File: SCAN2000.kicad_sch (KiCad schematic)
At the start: 15 parts, among them J1 Conn_02x16_Row_Letter_First

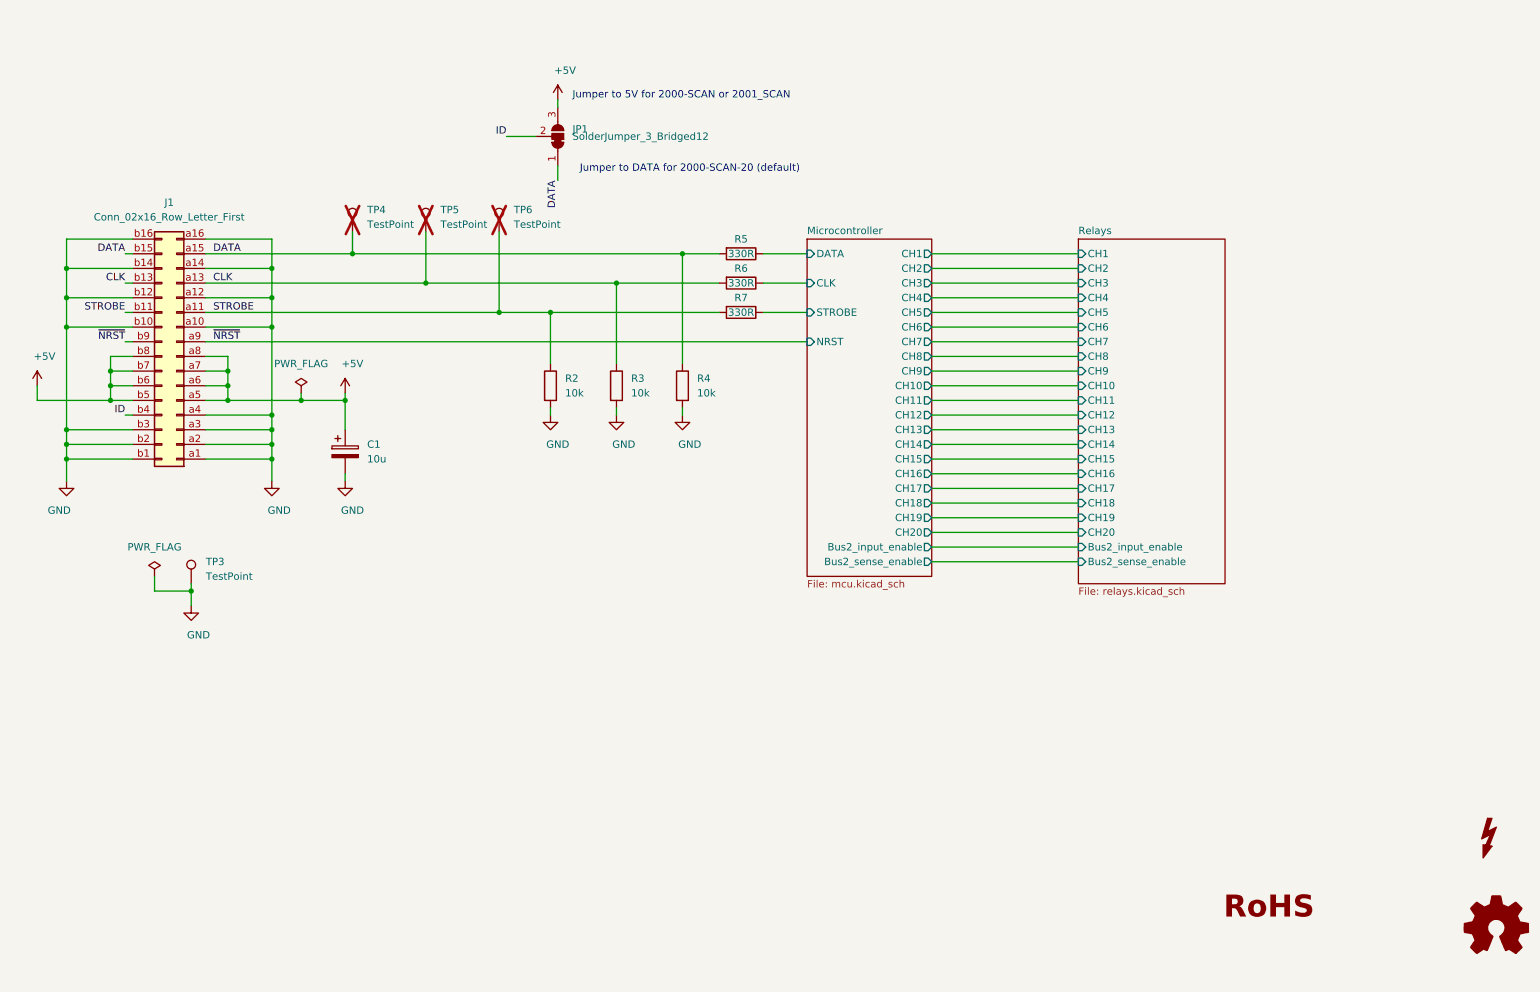
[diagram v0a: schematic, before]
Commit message: Replaced the STM32 microcontroller with an iCE40 FPGA
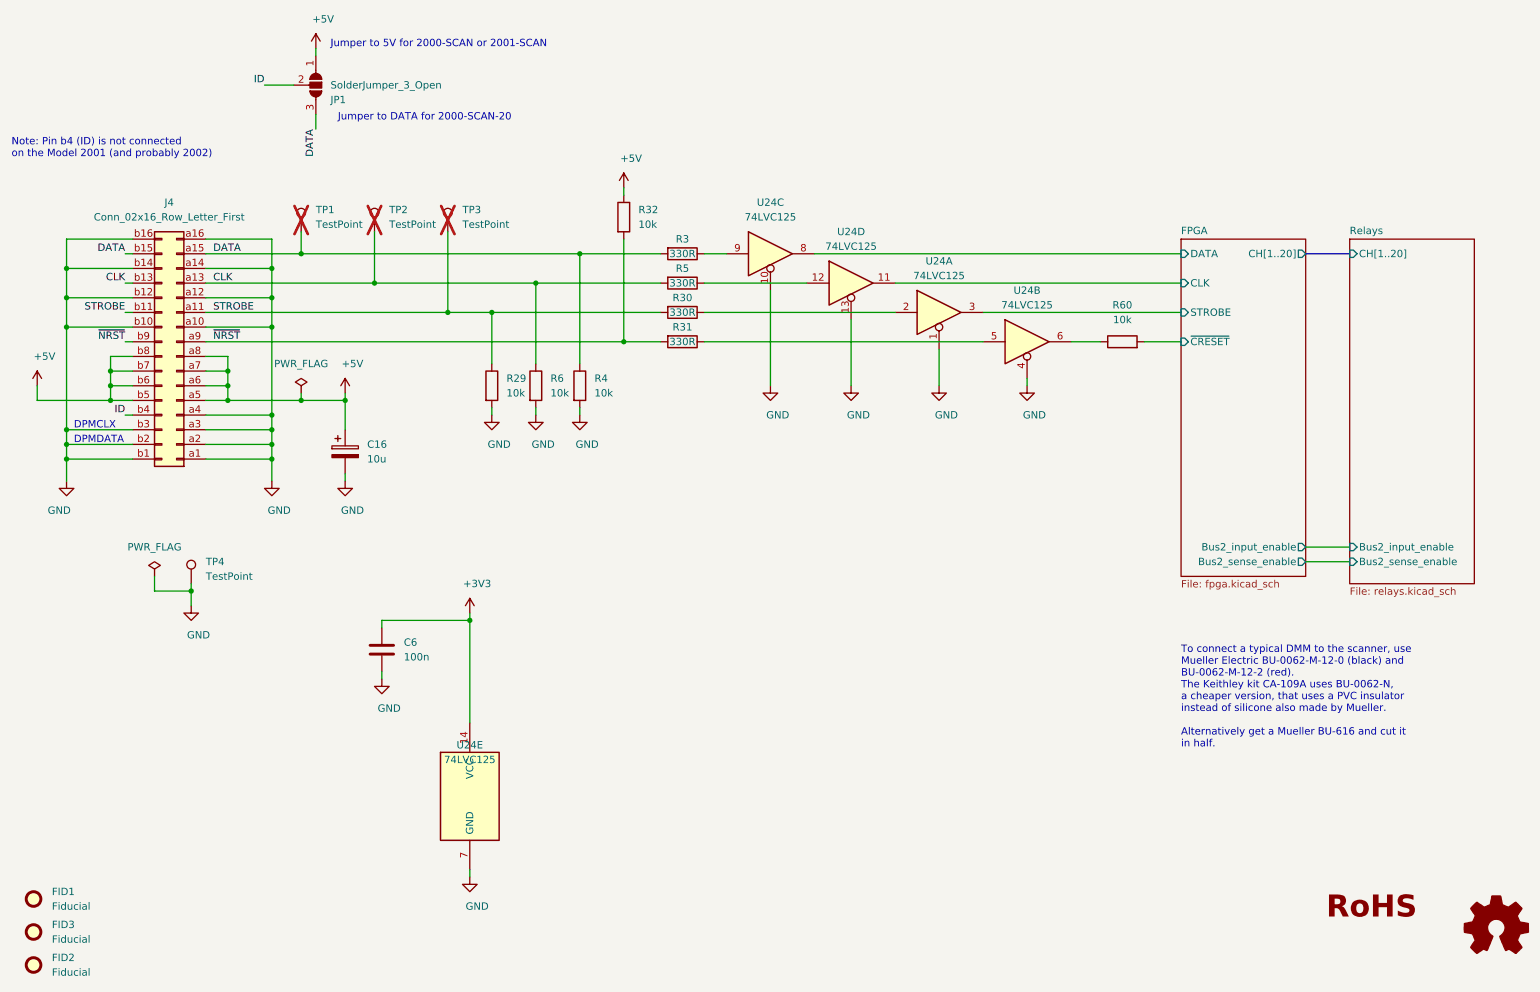
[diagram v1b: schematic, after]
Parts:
- removed SYM1: SYM_Flash_Small, Symbol:Symbol_HighVoltage_Triangle_17x15mm_Copper, symbol Graphic:SYM_Flash_Small
- added C6: 100n, Capacitor_SMD:C_0603_1608Metric, symbol Device:C
- added FID1, FID2, FID3: Fiducial, Fiducial:Fiducial_0.5mm_Mask1mm, symbol Mechanical:Fiducial
- added R31: 330R, Resistor_SMD:R_0603_1608Metric, symbol Device:R
- added R32, R60: 10k, Resistor_SMD:R_0603_1608Metric, symbol Device:R
- added U24: 74LVC125, Package_SO:TSSOP-14_4.4x5mm_P0.65mm, symbol 74xx:74LVC125
- J4: renamed from J1; Alternative (none) -> Harting 09272326804; RoHS Yes -> (none); Temperature Tstorage = –55 °C to 125 °C -> (none)
- JP1: value SolderJumper_3_Bridged12 -> SolderJumper_3_Open; footprint Jumper:SolderJumper-3_P1.3mm_Bridged12_Pad1.0x1.5mm_NumberLabels -> Jumper:SolderJumper-3_P1.3mm_Open_Pad1.0x1.5mm; symbol Jumper:SolderJumper_3_Bridged12 -> Jumper:SolderJumper_3_Open; Config (none) -> do not fit; now in the parts list
- R29: renamed from R2; Note (none) -> 5% or better; PN CRCW060310K0JNEB -> CRCW060310K0JNEA
- R3: renamed from R5; Alternative (none) -> Yageo AC0603JR-07330RL or AC0603FR-07330RL; Note (none) -> 5% or better; PN CRCW0603330RJNEB -> CRCW0603330RJNEA
- R30: renamed from R7; Alternative (none) -> Yageo AC0603JR-07330RL or AC0603FR-07330RL; Note (none) -> 5% or better; PN CRCW0603330RJNEB -> CRCW0603330RJNEA
- R4: Note (none) -> 5% or better; PN CRCW060310K0JNEB -> CRCW060310K0JNEA
- R5: renamed from R6; Alternative (none) -> Yageo AC0603JR-07330RL or AC0603FR-07330RL; Note (none) -> 5% or better; PN CRCW0603330RJNEB -> CRCW0603330RJNEA
- R6: renamed from R3; Note (none) -> 5% or better; PN CRCW060310K0JNEB -> CRCW060310K0JNEA
- TP1: renamed from TP4; DNP (none) -> 1; Note Solder only for debugging -> Fit only for debugging
- TP2: renamed from TP5; DNP (none) -> 1; Note Solder only for debugging -> Fit only for debugging
- TP3: renamed from TP6; DNP (none) -> 1; Note Solder only for debugging -> Fit only for debugging
- TP4: renamed from TP3; DNP (none) -> 1; Note (none) -> Fit only for debugging
- renumbered C1 to C16, LOGO2 to LOGO1
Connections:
- net +5V: now also JP1.1 (A), R32.1; no longer JP1.3 (B)
- net DATA: now also JP1.3 (B); no longer JP1.1 (A)
- net GND: now also C6.2, U24.1, U24.10, U24.13, U24.4, U24.7 (GND)
- net FPGA/CLK: now also U24.11; no longer R5.1
- net FPGA/DATA: now also U24.8; no longer R3.1
- net FPGA/STROBE: now also U24.3; no longer R30.1
- net ~{NRST}: now also R31.2, R32.2
- new net: R3.1, U24.9
- new net: R5.1, U24.12
- new net: R30.1, U24.2
- new net: R31.1, U24.5
- new net: R60.1, U24.6
- new net +3V3: C6.1, U24.14 (VCC)
- new net FPGA/~{CRESET}: R60.2
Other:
- sheet Microcontroller renamed FPGA
- sheet FPGA: file mcu.kicad_sch -> fpga.kicad_sch
- sheet FPGA ports: added CH[1..20], ~{CRESET}; removed CH1, CH10, CH11, CH12, CH13, CH14, CH15, CH16, CH17, CH18, CH19, CH2, CH20, CH3, CH4, CH5, CH6, CH7, CH8, CH9, NRST
- sheet Relays ports: added CH[1..20]; removed CH1, CH10, CH11, CH12, CH13, CH14, CH15, CH16, CH17, CH18, CH19, CH2, CH20, CH3, CH4, CH5, CH6, CH7, CH8, CH9
- note added: "DPMCLX"
- note added: "DPMDATA"
- note added: "Jumper to 5V for 2000-SCAN or 2001-SCAN"
- note added: "Jumper to DATA for 2000-SCAN-20"
- note added: "Note: Pin b4 (ID) is not connected on the Model 2001 (and probably 2002)"
- note added: "To connect a typical DMM to the scanner, use Mueller Electric BU‐0062-M-12-0 (black) and BU‐0062-M-12-2 (red). The Keithley kit CA-109A uses BU‐0062‐N, a cheaper version, that uses a PVC insulator instead of silicone also made by Mueller. Alternatively get a Mueller BU-616 and cut it in half."
- note removed: "Jumper to 5V for 2000-SCAN or 2001_SCAN"
- note removed: "Jumper to DATA for 2000-SCAN-20 (default)"
- moved on the sheet: R29, R3, R30, R4, R5, R6, TP1, TP2, TP3

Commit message: Updated BOM properties
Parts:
- J4: Digikey# (none) -> 09272326804-ND
- JP1: now left out of the parts list
- TP4: now not fitted
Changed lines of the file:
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@@
+			)
+		)
+		(property "Digikey#" "09272326804-ND"
+			(at 46.99 74.93 0)
+			(effects
+				(font
+					(size 1.27 1.27)
+				)
+				(hide yes)
 			)
 		)
@@
 		(unit 1)
 		(exclude_from_sim no)
-		(in_bom yes)
+		(in_bom no)
 		(on_board yes)
 		(dnp no)
@@
 		(in_bom yes)
 		(on_board yes)
-		(dnp no)
+		(dnp yes)
 		(property "Reference" "TP4"
 			(at 52.07 110.49 0)
